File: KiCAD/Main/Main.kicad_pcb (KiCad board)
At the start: 4 copper layers, 60 x 150 mm, 115 parts, among them J1 Micro_SD_Card_Det2, J2 Screw_Terminal_01x09, J3 Screw_Terminal_01x09, J4 USB_C_Receptacle_USB2.0_16P, J5 Conn_02x04_Counter_Clockwise, J6 Conn_01x03, J8 Conn_Coaxial, J9 Conn_Coaxial, Q1 AO3400A, Q2 AO3400A, Q3 AO3400A, Q4 2N7002, SW1 RESET, SW2 USER, U1 LM2596S-3.3, U11 BMP390L, U12 BMP390L, U13 BMP390L, U14 BMI270, U15 BMI270, U16 BMI270, U17 SHT4x, U2 TPS2121RUXR, U3 LIS2MDL, U4 STM32H750VBTx, U5 MAX-M8Q, U7 ISM6HG256x, Y2 SiT8008xx-2x-xxE (25MHz)

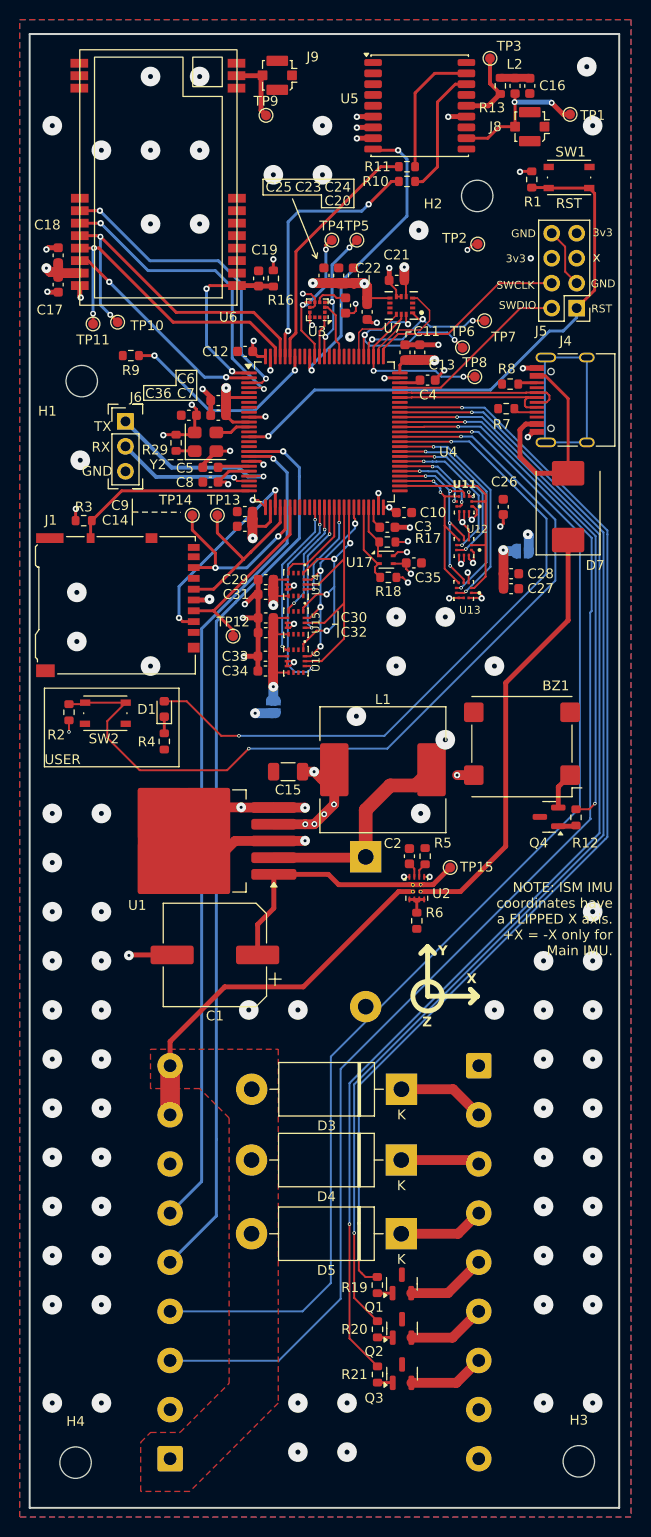
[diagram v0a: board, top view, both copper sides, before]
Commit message: save after realizing branch was not switched to layoutv2
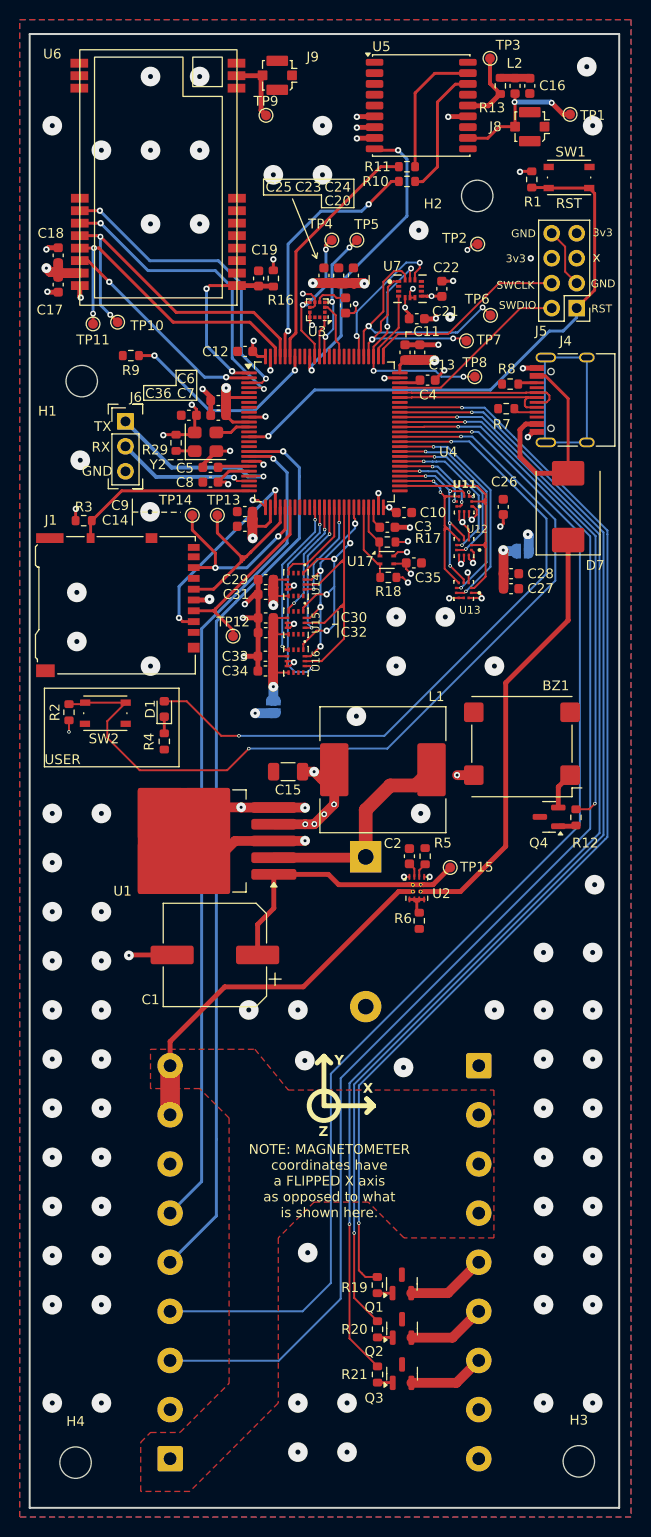
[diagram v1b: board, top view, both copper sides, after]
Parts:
- removed D3, D4, D5: 1N5820, Diode_THT:D_DO-201AD_P15.24mm_Horizontal
- U5: value MAX-M8Q -> MAX-M10S
- U6: value ~ -> E22-900T22S
- moved C22 7.96 mm to (149.7, 56.6), turned to -90 degrees
- moved C21 4.41 mm to (147.1, 59.6), turned to 180 degrees
- moved TP6 4.36 mm to (154.6, 59.3)
- moved TP7 2.76 mm to (152.2, 61.9)
- moved U7 1.92 mm to (146.4, 56.6), turned to 0 degrees
- moved R6 0.25 mm to (147.3, 120.9)
- moved U5 0.15 mm to (147.6, 38.0)
- moved U17 0.06 mm to (144.1, 84.2)
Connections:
- J2 pad 1: Net-(D3-A) -> Net-(J2-7.4V_IN)
- J2 pad 8: Net-(D3-A) -> Net-(J2-7.4V_IN)
- J2 pad 9: Net-(D3-A) -> Net-(J2-7.4V_IN)
- J3 pad 2: Net-(D3-K) -> Net-(J2-7.4V_IN)
- J3 pad 3: Net-(D4-K) -> Net-(J2-7.4V_IN)
- J3 pad 4: Net-(D5-K) -> Net-(J2-7.4V_IN)
- U2 pad 2: Net-(D3-A) -> Net-(J2-7.4V_IN)
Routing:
- net Net-(J2-7.4V_IN): track 0.00 -> 38.8 mm
- net Net-(D3-A): track 38.2 -> 0.00 mm
- net Net-(D3-K): track 8.95 -> 0.00 mm
- net Net-(D5-K): track 8.76 -> 0.00 mm
- net Net-(D4-K): track 8.06 -> 0.00 mm
- net /IMUs/ISM_CS: track 7.07 -> 15.1 mm, vias 0 -> 2
- net /IMUs/ISM_SCK: track 17.5 -> 23.9 mm, vias 2 -> 4
- net /IMUs/ISM_MOSI: track 20.3 -> 25.8 mm, vias 3 -> 2
- net /IMUs/ISM_INT: track 10.5 -> 6.99 mm
- net /IMUs/ISM_MISO: track 16.0 -> 19.2 mm, vias 3 -> 2
- net +3V3: track 113.5 -> 110.5 mm, vias 38 -> 39
- net /Barometer/BMP390_SCK: track 22.3 -> 23.6 mm
- net /GPS/GPS_SDA: track 26.8 -> 25.5 mm
- net /Microcontroller/SIMU CLK: track 28.5 -> 29.6 mm
- net /Microcontroller/SD_CLK: track 18.4 -> 19.4 mm
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- added copper zone on F.Cu, net Net-(J2-7.4V_IN)
- removed copper zone on F.Cu, net Net-(D3-A)
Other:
- board text added: "NOTE: MAGNETOMETER coordinates have a FLIPPED X axis as opposed to what is shown here."
- board text removed: "NOTE: ISM IMU coordinates have a FLIPPED X axis. +X = -X only for Main IMU."

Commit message: Edit PCB Layout to increase min hole size and decrease price, prepare production files, prepare for main branch merge
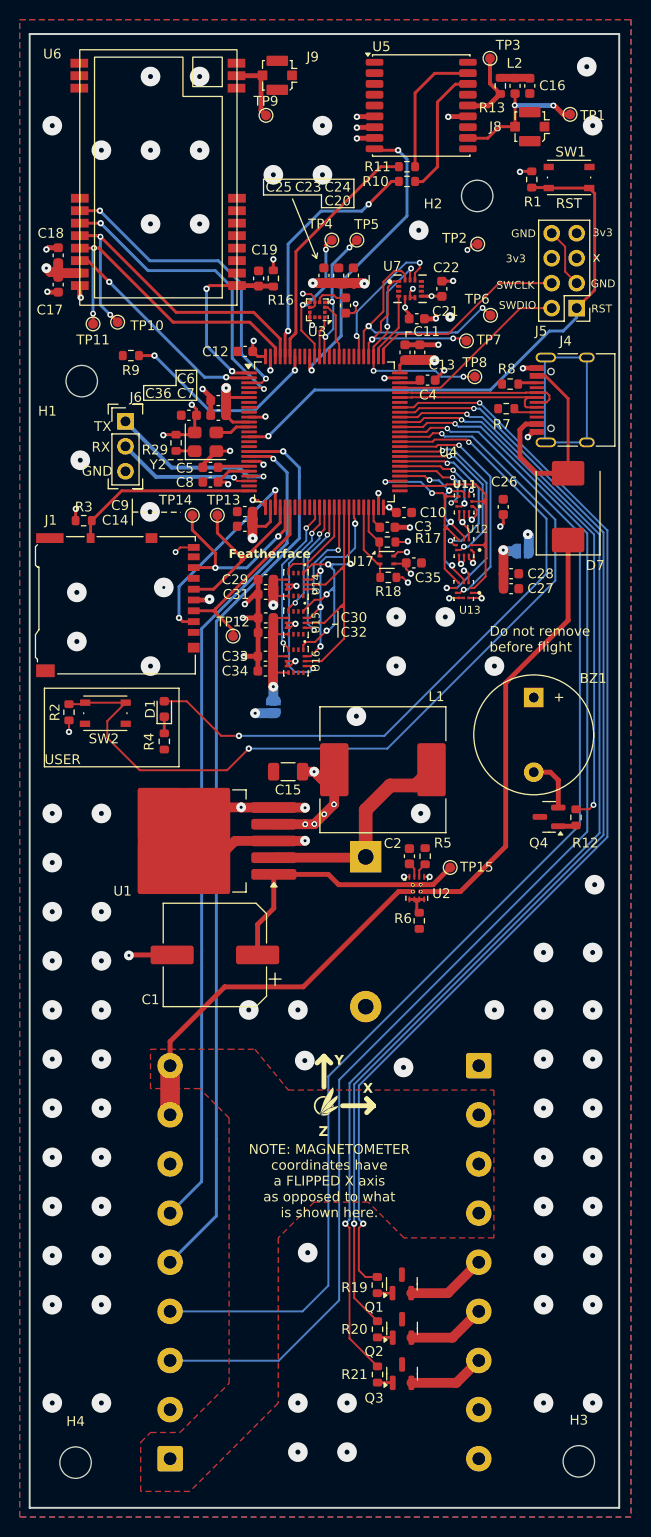
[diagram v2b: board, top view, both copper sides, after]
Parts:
- added G***: LOGO, temp:1P3jn1GVe0o663oW61IFHCrs1ryg256Phj2hFYreBh484vDH7kl, F.Cu at (137.8, 139.3)
- added G***: LOGO, LRI:LOGO, B.Cu at (137.7, 71.0)
- BZ1: footprint Buzzer_Beeper:MagneticBuzzer_PUI_SMT-1028-T-2-R -> Buzzer_Beeper:Buzzer_12x9.5RM7.6
- moved BZ1 5.14 mm to (159.0, 98.2), turned to -90 degrees
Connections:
- BZ1 pad 1: Net-(BZ1-+) -> +3V3
- BZ1 pad 2: +3V3 -> Net-(BZ1--)
- Q4 pad 2: Net-(BZ1-+) -> Net-(BZ1--)
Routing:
- net Net-(BZ1--): track 0.00 -> 5.63 mm
- net Net-(BZ1-+): track 3.80 -> 0.00 mm
- net GND: track 101.2 -> 104.5 mm, vias 118 -> 119
- net /Barometer/BMP390_MISO: track 19.2 -> 22.2 mm
- net /Barometer/BMP390_CS3: track 21.9 -> 24.3 mm
- net /Microcontroller/SIMU MISO: track 25.4 -> 27.3 mm
- net /Barometer/BMP390_CS2: track 15.8 -> 17.5 mm
- net +3V3: track 110.5 -> 108.8 mm, vias 39 -> 37
- net /Barometer/BMP390_CS1: track 7.91 -> 9.44 mm
- net /Microcontroller/SIMU CS1: track 10.3 -> 11.5 mm
- net /Barometer/BMP390_MOSI: track 20.0 -> 21.2 mm
- net /Microcontroller/SIMU MOSI: track 21.7 -> 22.9 mm
- net /Barometer/BMP390 INT1: track 9.36 -> 10.4 mm
- net /Barometer/BMP390 INT3: track 23.5 -> 24.4 mm
- net /Microcontroller/SIMU CLK: track 29.6 -> 28.8 mm
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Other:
- board text added: "Do not remove before flight"
- board text added: "Featherface"
- board text added: "Liquid Rocketry Illinois University of Illinois Urbana-Champaign"

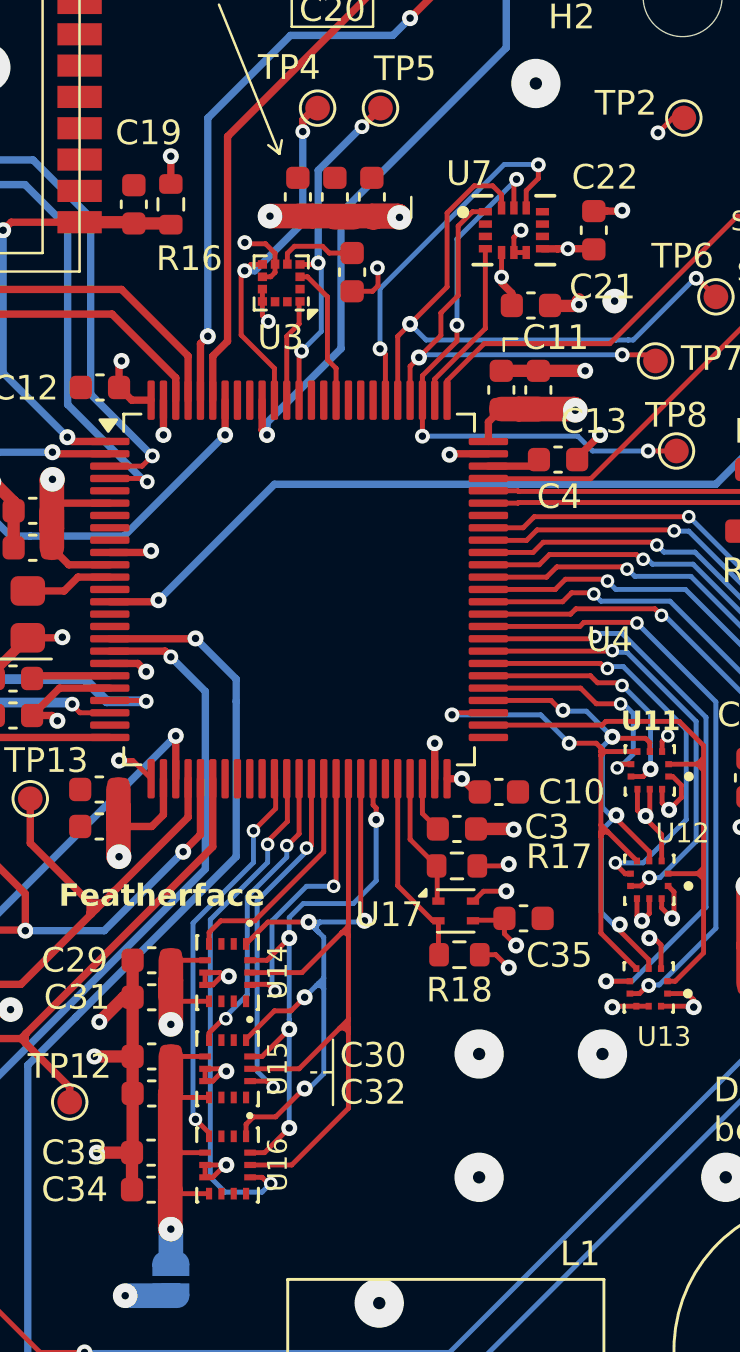
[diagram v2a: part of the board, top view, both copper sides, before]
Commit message: Reorganize libraries into LRI.pretty, replace BMI270 with BMI323
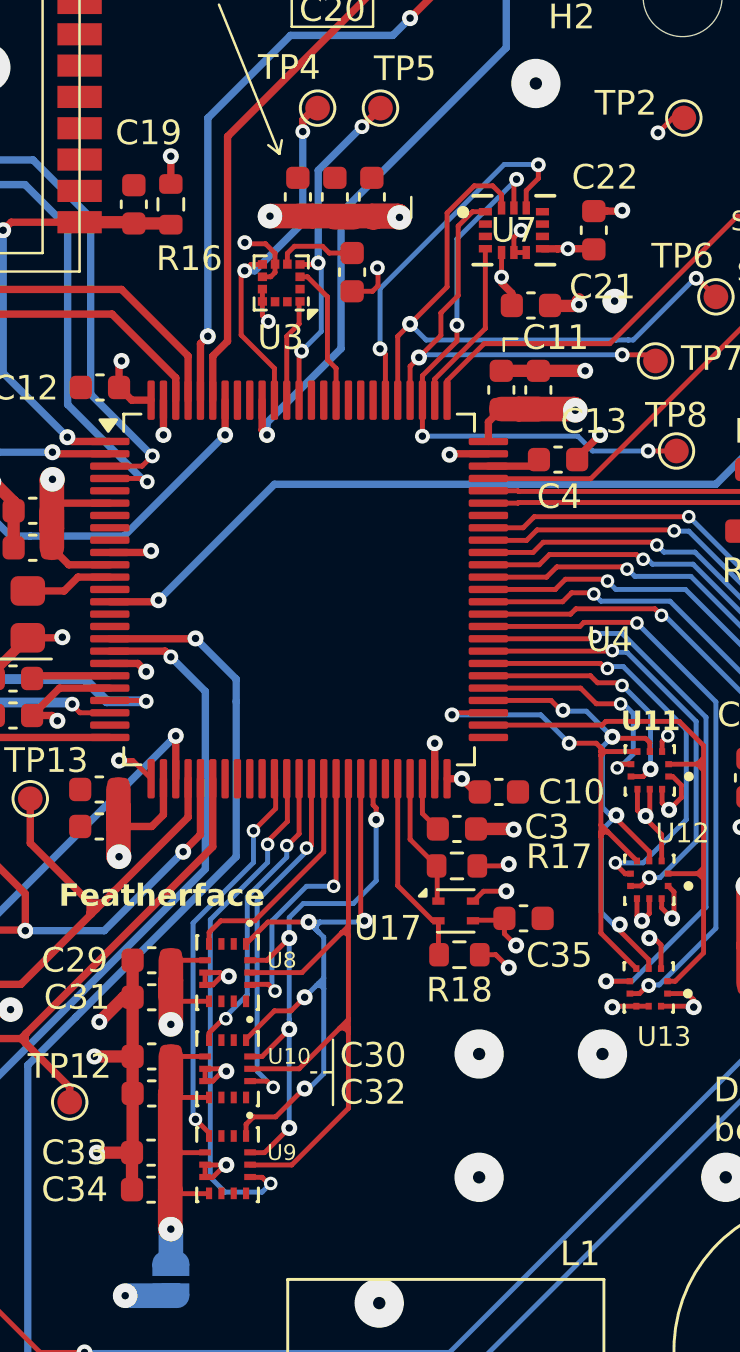
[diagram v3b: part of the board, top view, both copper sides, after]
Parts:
- removed U14, U15, U16: BMI270, LRI:XDCR_BMI270
- added U10: ~, LRI:BMI323, F.Cu at (134.8, 90.6)
- added U8: ~, LRI:BMI323, F.Cu at (134.8, 86.7)
- added U9: ~, LRI:BMI323, F.Cu at (134.8, 94.5)
- U7: footprint LRI:ISM6 -> LRI:ISM6HG256XTR
